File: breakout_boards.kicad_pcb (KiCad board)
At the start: 2 copper layers, 21.8 x 11.7 mm, 10 parts, among them J1 Conn_01x04, J2 Conn_01x04

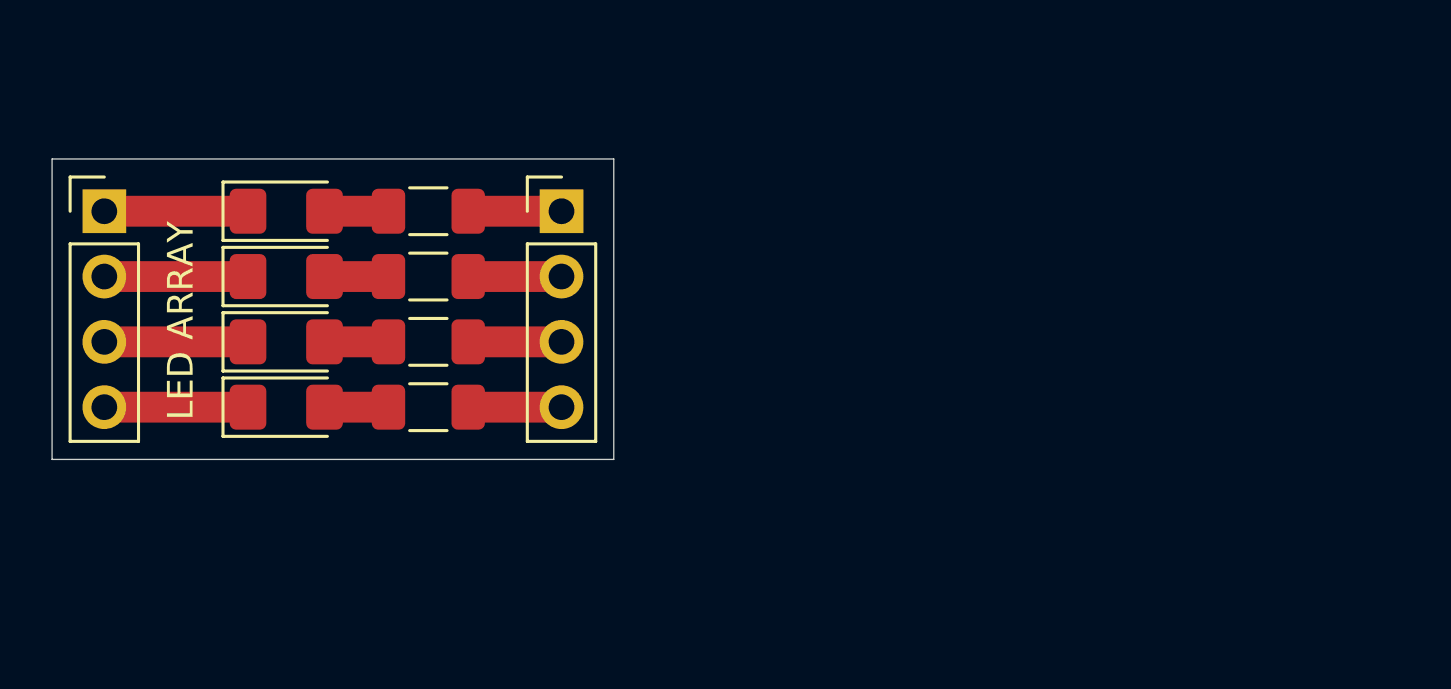
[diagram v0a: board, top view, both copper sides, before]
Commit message: updated gitignore and added single keyboard switch, with debouncing
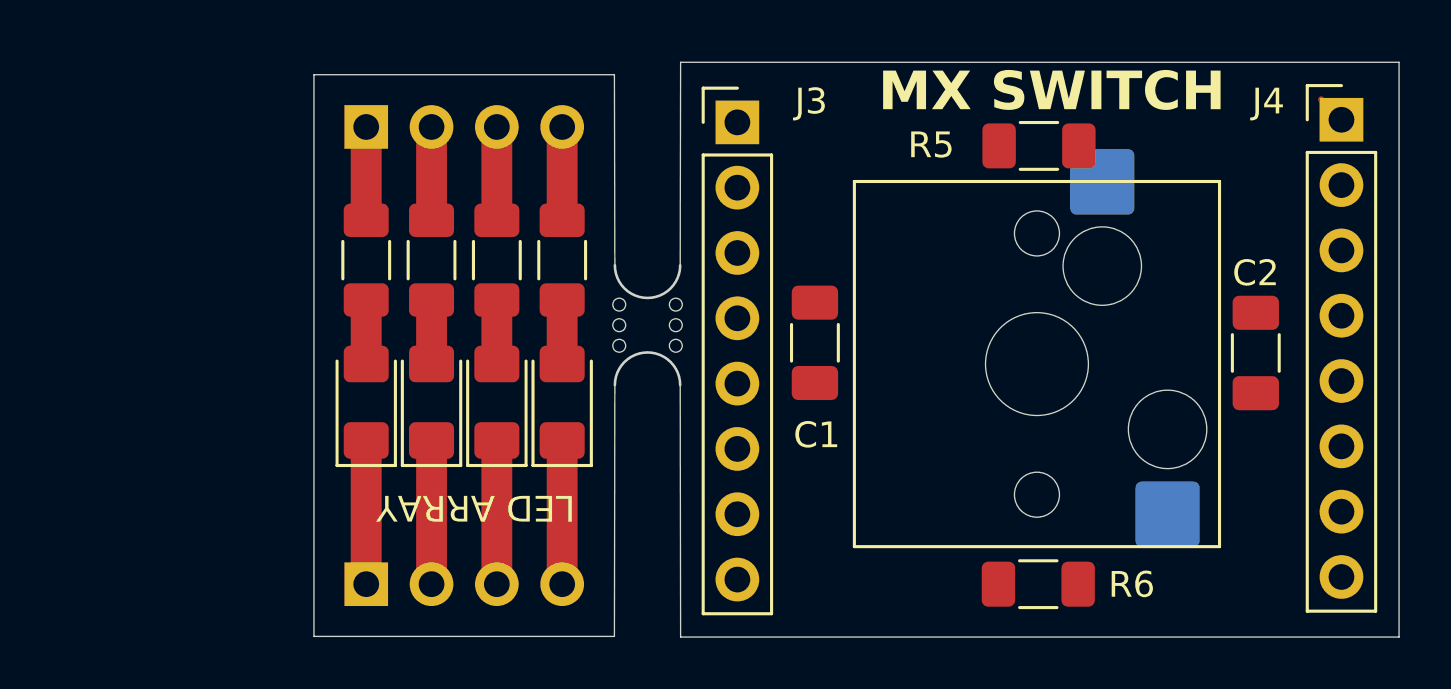
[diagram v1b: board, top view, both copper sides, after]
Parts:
- added C1: C_Small, Capacitor_SMD:C_1206_3216Metric_Pad1.33x1.80mm_HandSolder, F.Cu at (53.0, 25.4)
- added C2: C_Small, Capacitor_SMD:C_1206_3216Metric_Pad1.33x1.80mm_HandSolder, F.Cu at (70.2, 25.8)
- added H1: MountingHole, Panelization:mouse-bite-2.54mm-slot, F.Cu at (46.5, 24.8)
- added J3: Conn_01x08, Connector_PinHeader_2.54mm:PinHeader_1x08_P2.54mm_Vertical, F.Cu at (50.0, 16.9)
- added J4: Conn_01x08, Connector_PinHeader_2.54mm:PinHeader_1x08_P2.54mm_Vertical, F.Cu at (73.5, 16.8)
- added R5: R_Small, Resistor_SMD:R_1206_3216Metric_Pad1.30x1.75mm_HandSolder, F.Cu at (61.7, 17.8)
- added R6: R_Small, Resistor_SMD:R_1206_3216Metric_Pad1.30x1.75mm_HandSolder, F.Cu at (61.7, 34.8)
- added SW7: SW_Push, Button_Switch_Keyboard:SW_Hotswap_Kailh_MX_1.00u, F.Cu at (61.7, 26.3)
- J1, J2: moved to B.Cu
- moved J1 17.7 mm to (35.6, 34.8), turned to -90 degrees
- moved D4 10.7 mm to (43.2, 27.7), turned to 90 degrees
- moved D3 8.52 mm to (40.7, 27.7), turned to 90 degrees
- moved J2 8.27 mm to (35.6, 17.0), turned to -90 degrees
- moved D1 8.05 mm to (35.6, 27.7), turned to 90 degrees
- moved R4 7.73 mm to (43.2, 22.2), turned to 90 degrees
- moved D2 7.47 mm to (38.1, 27.7), turned to 90 degrees
- moved R3 4.15 mm to (40.7, 22.2), turned to 90 degrees
- moved R1 3.07 mm to (35.6, 22.2), turned to 90 degrees
- moved R2 0.65 mm to (38.1, 22.2), turned to 90 degrees
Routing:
- net Net-(J3-Pin_1): track 0.00 -> 1.17 mm
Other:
- board size 21.8 x 11.7 mm -> 42.2 x 22.4 mm
- board text added: "MX SWITCH"

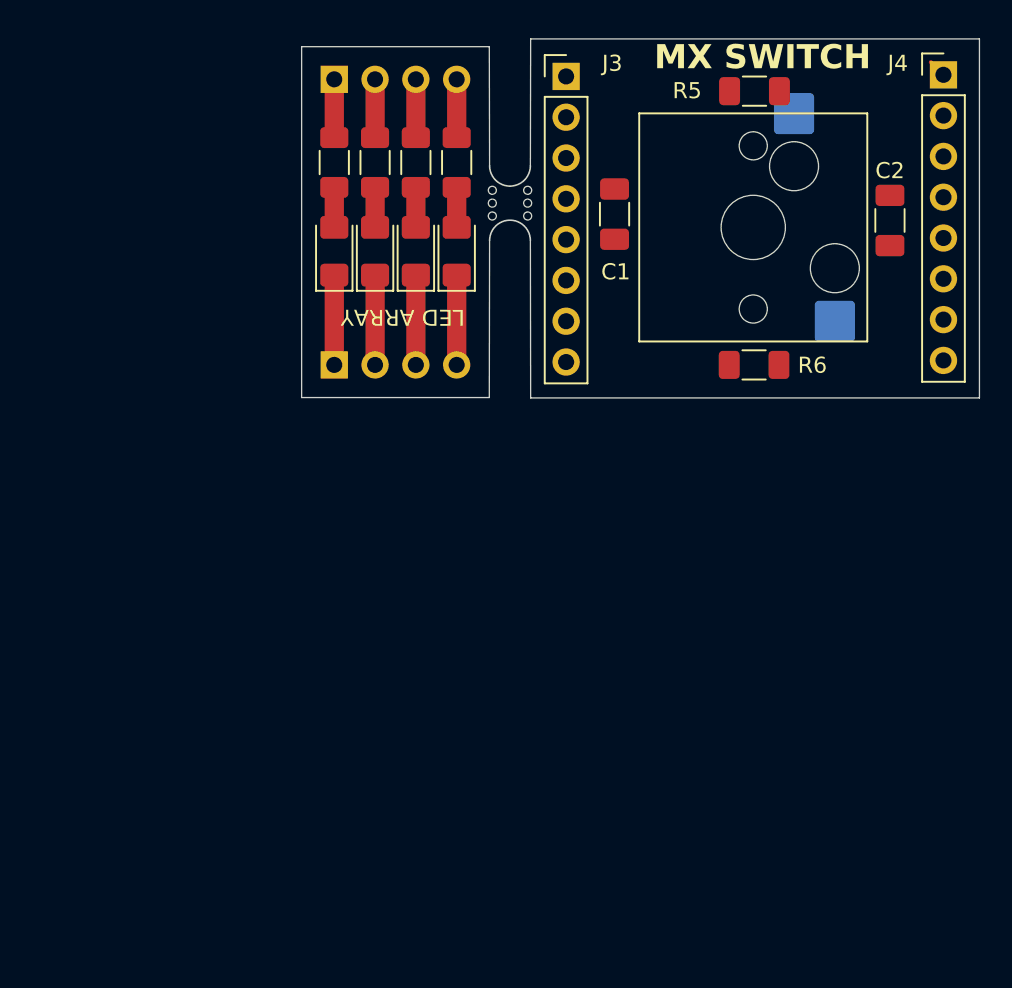
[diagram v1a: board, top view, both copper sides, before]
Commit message: added matrix keyboard pending to remove unused pins and use more header pins
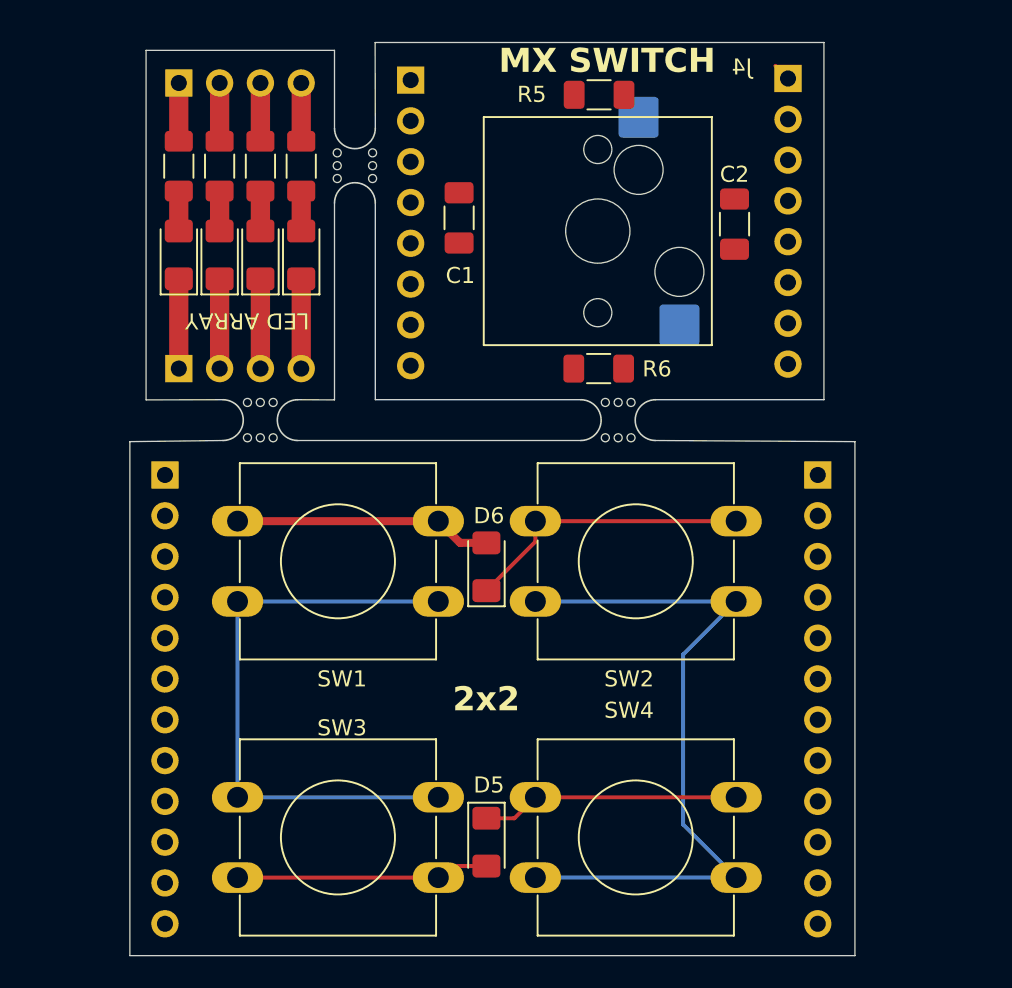
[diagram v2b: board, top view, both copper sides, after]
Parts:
- removed H1: MountingHole, Panelization:mouse-bite-2.54mm-slot
- added D5: D_Small, Diode_SMD:D_1206_3216Metric_Pad1.42x1.75mm_HandSolder, F.Cu at (45.1, 64.5)
- added D6: D_Small, Diode_SMD:D_1206_3216Metric_Pad1.42x1.75mm_HandSolder, F.Cu at (45.1, 47.4)
- added J5: Conn_01x12, Connector_PinHeader_2.54mm:PinHeader_1x12_P2.54mm_Vertical, B.Cu at (25.0, 41.7)
- added J6: Conn_01x12, Connector_PinHeader_2.54mm:PinHeader_1x12_P2.54mm_Vertical, B.Cu at (65.7, 41.7)
- added SW1: SW_Push_45deg, Button_Switch_THT:SW_PUSH-12mm, F.Cu at (29.6, 44.5)
- added SW2: SW_Push_45deg, Button_Switch_THT:SW_PUSH-12mm, F.Cu at (48.1, 44.5)
- added SW3: SW_Push_45deg, Button_Switch_THT:SW_PUSH-12mm, F.Cu at (42.1, 66.7)
- added SW4: SW_Push_45deg, Button_Switch_THT:SW_PUSH-12mm, F.Cu at (48.1, 61.7)
- added mouse-bite-2.54mm-slot: VAL**, Panelization:mouse-bite-2.54mm-slot, F.Cu at (36.9, 22.4)
- added mouse-bite-2.54mm-slot: VAL**, Panelization:mouse-bite-2.54mm-slot, F.Cu at (31.0, 38.3)
- added mouse-bite-2.54mm-slot: VAL**, Panelization:mouse-bite-2.54mm-slot, F.Cu at (53.3, 38.3)
- J3, J4: moved to B.Cu
- moved C1 9.68 mm to (43.4, 25.7)
- moved SW7 9.68 mm to (52.0, 26.5)
- moved C2 9.68 mm to (60.5, 26.1)
- moved D1 9.68 mm to (25.9, 28.0)
- moved D2 9.68 mm to (28.4, 28.0)
- moved D3 9.68 mm to (31.0, 28.0)
- moved D4 9.68 mm to (33.5, 28.0)
- moved J1 9.68 mm to (25.9, 35.1)
- moved J2 9.68 mm to (25.9, 17.3)
- moved J3 9.68 mm to (40.3, 17.1), turned to 180 degrees
- moved J4 9.68 mm to (63.8, 17.0), turned to 180 degrees
- moved R1 9.68 mm to (25.9, 22.5)
- moved R2 9.68 mm to (28.4, 22.5)
- moved R3 9.68 mm to (31.0, 22.5)
- moved R4 9.68 mm to (33.5, 22.5)
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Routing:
- net Net-(SW2-Pad2): track 0.00 -> 44.9 mm
- net Net-(SW1-Pad2): track 0.00 -> 37.2 mm
- net Net-(D6-K): track 0.00 -> 18.1 mm
- net Net-(D5-K): track 0.00 -> 16.1 mm
- net Net-(D6-A): track 0.00 -> 16.1 mm
- net Net-(D5-A): track 0.00 -> 15.8 mm
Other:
- board size 42.2 x 22.4 mm -> 45.1 x 56.8 mm
- board text added: "2x2"

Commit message: refactored pcb, added led matrix
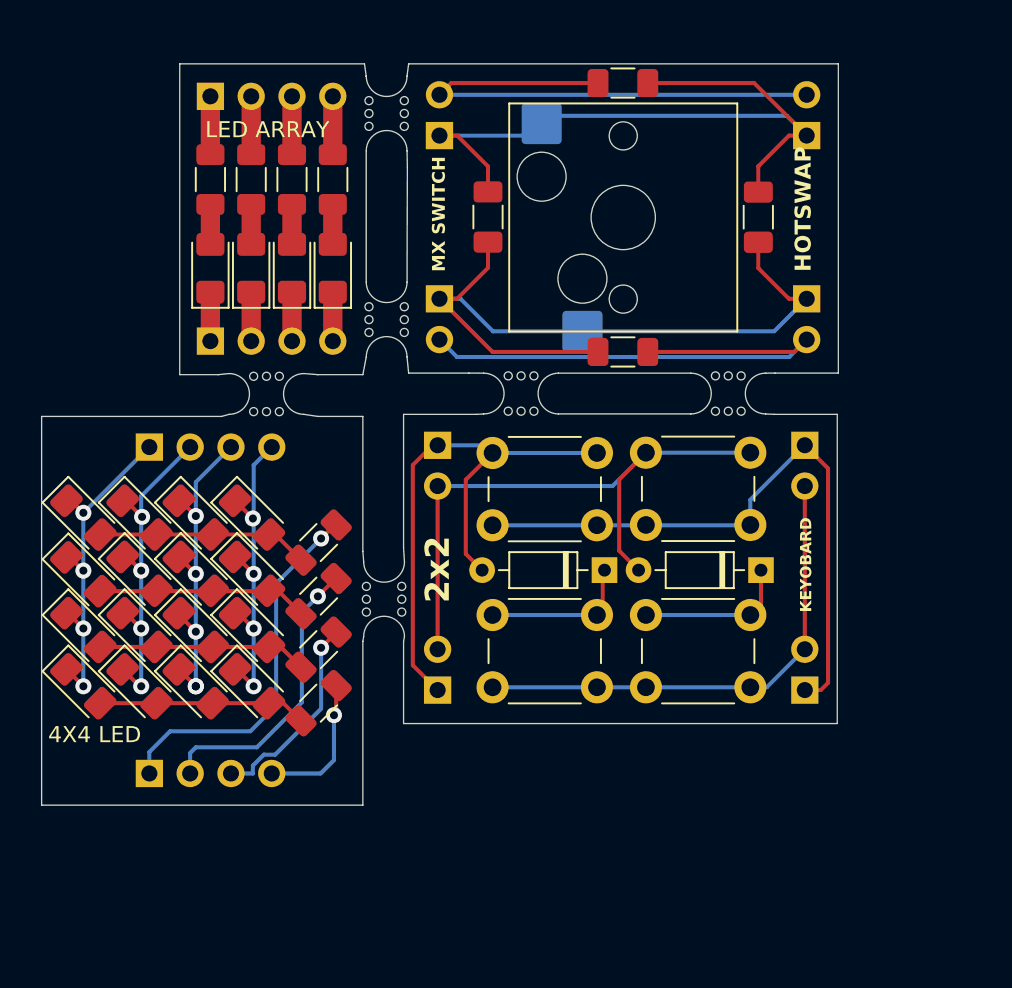
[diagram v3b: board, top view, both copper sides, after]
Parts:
- removed mouse-bite-2.54mm-slot (x3): VAL**, Panelization:mouse-bite-2.54mm-slot
- added D10: D_45deg, LED_SMD:LED_1206_3216Metric_Pad1.42x1.75mm_HandSolder, F.Cu at (27.0, 51.3)
- added D11: D_45deg, LED_SMD:LED_1206_3216Metric_Pad1.42x1.75mm_HandSolder, F.Cu at (23.5, 54.8)
- added D12: D_45deg, LED_SMD:LED_1206_3216Metric_Pad1.42x1.75mm_HandSolder, F.Cu at (23.5, 51.3)
- added D13: D_45deg, LED_SMD:LED_1206_3216Metric_Pad1.42x1.75mm_HandSolder, F.Cu at (20.0, 54.8)
- added D14: D_45deg, LED_SMD:LED_1206_3216Metric_Pad1.42x1.75mm_HandSolder, F.Cu at (20.0, 51.3)
- added D15: D_45deg, LED_SMD:LED_1206_3216Metric_Pad1.42x1.75mm_HandSolder, F.Cu at (30.5, 47.8)
- added D16: D_45deg, LED_SMD:LED_1206_3216Metric_Pad1.42x1.75mm_HandSolder, F.Cu at (30.5, 44.3)
- added D17: D_45deg, LED_SMD:LED_1206_3216Metric_Pad1.42x1.75mm_HandSolder, F.Cu at (27.0, 47.8)
- added D18: D_45deg, LED_SMD:LED_1206_3216Metric_Pad1.42x1.75mm_HandSolder, F.Cu at (27.0, 44.3)
- added D19: D_45deg, LED_SMD:LED_1206_3216Metric_Pad1.42x1.75mm_HandSolder, F.Cu at (23.5, 47.8)
- added D20: D_45deg, LED_SMD:LED_1206_3216Metric_Pad1.42x1.75mm_HandSolder, F.Cu at (23.5, 44.3)
- added D21: D_45deg, LED_SMD:LED_1206_3216Metric_Pad1.42x1.75mm_HandSolder, F.Cu at (20.0, 47.9)
- added D22: D_45deg, LED_SMD:LED_1206_3216Metric_Pad1.42x1.75mm_HandSolder, F.Cu at (20.0, 44.3)
- added D7: D_45deg, LED_SMD:LED_1206_3216Metric_Pad1.42x1.75mm_HandSolder, F.Cu at (30.5, 54.8)
- added D8: D_45deg, LED_SMD:LED_1206_3216Metric_Pad1.42x1.75mm_HandSolder, F.Cu at (27.0, 54.8)
- added D9: D_45deg, LED_SMD:LED_1206_3216Metric_Pad1.42x1.75mm_HandSolder, F.Cu at (30.5, 51.3)
- added H1: MountingHole, Panelization:mouse-bite-2.54mm-slot, F.Cu at (38.8, 19.2)
- added H2: MountingHole, Panelization:mouse-bite-2.54mm-slot, F.Cu at (38.8, 32.0)
- added H3: MountingHole, Panelization:mouse-bite-2.54mm-slot, F.Cu at (47.2, 36.6)
- added H4: MountingHole, Panelization:mouse-bite-2.54mm-slot, F.Cu at (60.1, 36.6)
- added H5: MountingHole, Panelization:mouse-bite-2.54mm-slot, F.Cu at (31.4, 36.6)
- added H6: MountingHole, Panelization:mouse-bite-2.54mm-slot, F.Cu at (38.7, 49.4)
- added J10: Conn_01x02, Connector_PinHeader_2.54mm:PinHeader_1x02_P2.54mm_Vertical, B.Cu at (64.9, 39.8)
- added J11: Conn_01x04, Connector_PinHeader_2.54mm:PinHeader_1x04_P2.54mm_Vertical, B.Cu at (24.1, 60.3)
- added J12: Conn_01x04, Connector_PinHeader_2.54mm:PinHeader_1x04_P2.54mm_Vertical, B.Cu at (24.1, 39.9)
- added J7: Conn_01x02, Connector_PinHeader_2.54mm:PinHeader_1x02_P2.54mm_Vertical, B.Cu at (42.1, 30.7)
- added J8: Conn_01x02, Connector_PinHeader_2.54mm:PinHeader_1x02_P2.54mm_Vertical, B.Cu at (65.0, 30.7)
- added J9: Conn_01x02, Connector_PinHeader_2.54mm:PinHeader_1x02_P2.54mm_Vertical, B.Cu at (64.9, 55.1)
- added R10: R, Resistor_SMD:R_1206_3216Metric_Pad1.30x1.75mm_HandSolder, F.Cu at (34.6, 45.9)
- added R7: R, Resistor_SMD:R_1206_3216Metric_Pad1.30x1.75mm_HandSolder, F.Cu at (34.6, 55.9)
- added R8: R, Resistor_SMD:R_1206_3216Metric_Pad1.30x1.75mm_HandSolder, F.Cu at (34.6, 52.5)
- added R9: R, Resistor_SMD:R_1206_3216Metric_Pad1.30x1.75mm_HandSolder, F.Cu at (34.6, 49.2)
- D5, D6: footprint Diode_SMD:D_1206_3216Metric_Pad1.42x1.75mm_HandSolder -> Diode_THT:D_DO-35_SOD27_P7.62mm_Horizontal
- J3, J4: value Conn_01x08 -> Conn_01x02; footprint Connector_PinHeader_2.54mm:PinHeader_1x08_P2.54mm_Vertical -> Connector_PinHeader_2.54mm:PinHeader_1x02_P2.54mm_Vertical
- J5, J6: value Conn_01x12 -> Conn_01x02; footprint Connector_PinHeader_2.54mm:PinHeader_1x12_P2.54mm_Vertical -> Connector_PinHeader_2.54mm:PinHeader_1x02_P2.54mm_Vertical
- SW1, SW2, SW3, SW4: footprint Button_Switch_THT:SW_PUSH-12mm -> Button_Switch_THT:SW_PUSH_6mm
- moved SW3 29.4 mm to (55.0, 40.3), turned to 0 degrees
- moved J6 27.2 mm to (42.0, 55.1), turned to 0 degrees
- moved D5 24.1 mm to (62.2, 47.6), turned to 180 degrees
- moved C1 18.6 mm to (62.0, 25.6)
- moved J5 17.1 mm to (42.0, 39.8)
- moved SW1 16.4 mm to (45.4, 40.3)
- moved C2 15.4 mm to (45.2, 25.6)
- moved SW4 13.3 mm to (55.0, 50.4)
- moved D6 7.35 mm to (52.4, 47.6), turned to 180 degrees
- moved SW2 6.42 mm to (45.4, 50.4)
- moved J3 3.89 mm to (42.1, 20.5), turned to 0 degrees
- moved J4 3.74 mm to (65.0, 20.5), turned to 0 degrees
- moved J1 2.60 mm to (27.9, 33.3)
- moved D3 2.13 mm to (33.0, 28.8)
- moved D4 2.13 mm to (35.5, 28.8)
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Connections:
- C1 pad 1: Net-(J3-Pin_2) -> Net-(J3-Pin_1)
- C1 pad 2: Net-(J3-Pin_7) -> Net-(J7-Pin_1)
- C2 pad 1: Net-(J3-Pin_2) -> Net-(J3-Pin_1)
- C2 pad 2: Net-(J3-Pin_7) -> Net-(J7-Pin_1)
- J5 pad 2: Net-(D6-A) -> Net-(D5-A)
- J6 pad 1: unconnected-(J6-Pin_1-Pad1) -> Net-(D6-A)
- J6 pad 2: unconnected-(J6-Pin_2-Pad2) -> Net-(D5-A)
- R5 pad 1: Net-(J3-Pin_1) -> Net-(J3-Pin_2)
- R5 pad 2: Net-(J3-Pin_2) -> Net-(J3-Pin_1)
- R6 pad 1: Net-(J3-Pin_8) -> Net-(J7-Pin_2)
- R6 pad 2: Net-(J3-Pin_7) -> Net-(J7-Pin_1)
- SW7 pad 1: Net-(J3-Pin_7) -> Net-(J7-Pin_1)
- SW7 pad 2: Net-(J3-Pin_2) -> Net-(J3-Pin_1)
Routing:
- net Net-(J7-Pin_1): track 0.00 -> 46.6 mm
- net Net-(J3-Pin_1): track 1.17 -> 45.9 mm
- net Net-(J7-Pin_2): track 0.00 -> 34.0 mm
- net Net-(J3-Pin_2): track 0.00 -> 33.0 mm
- net Net-(J11-Pin_1): track 0.00 -> 23.3 mm, vias 0 -> 1
- net Net-(D5-A): track 15.8 -> 39.0 mm
- net Net-(D11-K): track 0.00 -> 22.4 mm, vias 0 -> 4
- net Net-(D13-K): track 0.00 -> 22.3 mm, vias 0 -> 4
- net Net-(D10-K): track 0.00 -> 21.8 mm, vias 0 -> 5
- net Net-(D15-K): track 0.00 -> 21.6 mm, vias 0 -> 4
- net Net-(D6-A): track 16.1 -> 35.2 mm
- net Net-(J11-Pin_2): track 0.00 -> 18.1 mm, vias 0 -> 1
- net Net-(J10-Pin_2): track 44.9 -> 30.6 mm
- net Net-(D16-A): track 0.00 -> 13.2 mm
- net Net-(D15-A): track 0.00 -> 13.1 mm
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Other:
- board size 45.1 x 56.8 mm -> 49.6 x 46.2 mm
- board text added: "4X4 LED"
- board text added: "HOTSWAP"
- board text added: "KEYOBARD"

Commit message: updated git ignored and generted fab outputs
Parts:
- moved SW3 0.44 mm to (55.4, 40.4)
- moved SW4 0.44 mm to (55.4, 50.5)
- moved D5 0.44 mm to (62.6, 47.7)
- moved D6 0.44 mm to (52.8, 47.7)
- moved H4 0.44 mm to (60.5, 36.7)
- moved J10 0.44 mm to (65.3, 39.9)
- moved J5 0.44 mm to (42.4, 39.9)
- moved J6 0.44 mm to (42.4, 55.2)
- moved J9 0.44 mm to (65.3, 55.2)
- moved SW1 0.44 mm to (45.9, 40.4)
- moved SW2 0.44 mm to (45.9, 50.5)
- moved H3 0.44 mm to (47.6, 36.7)
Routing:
- net Net-(J3-Pin_1): track 45.9 -> 44.2 mm
- net Net-(D6-A): track 35.2 -> 34.2 mm
- net Net-(D11-K): track 22.4 -> 21.7 mm
- net Net-(D13-K): track 22.3 -> 21.6 mm
- net Net-(D6-K): track 9.44 -> 8.94 mm
- net Net-(D10-K): track 21.8 -> 21.6 mm, vias 5 -> 4
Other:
- board size 49.6 x 46.2 mm -> 51.2 x 46.6 mm
